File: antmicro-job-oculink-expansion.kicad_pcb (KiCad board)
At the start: 4 copper layers, 20 x 60 mm, 25 parts, among them J1 OCuLink_x4_Amphenol_G14A42121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, J2 Plug_Samtec_ERM8_2x40_ERM8-04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, U1 MAX3373EEKA+

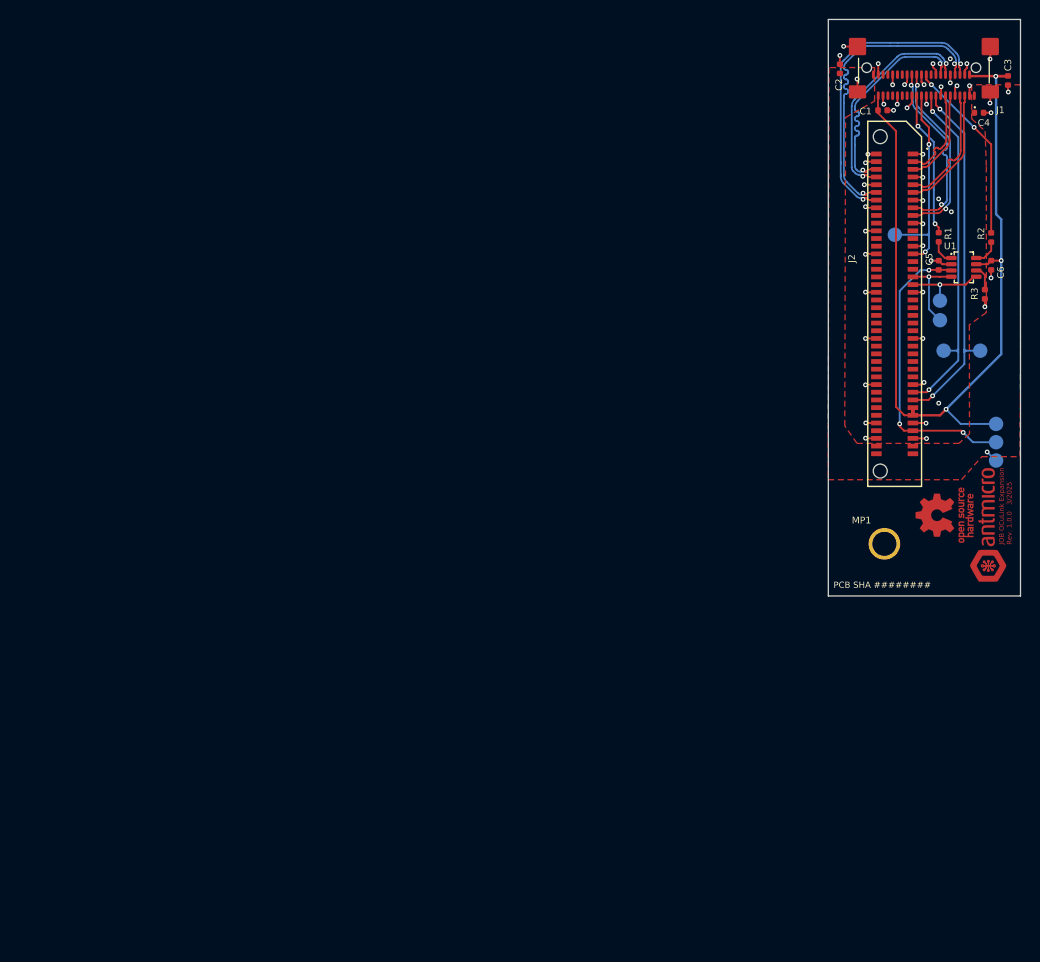
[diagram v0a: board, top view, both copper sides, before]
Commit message: [#74340] Update component placement
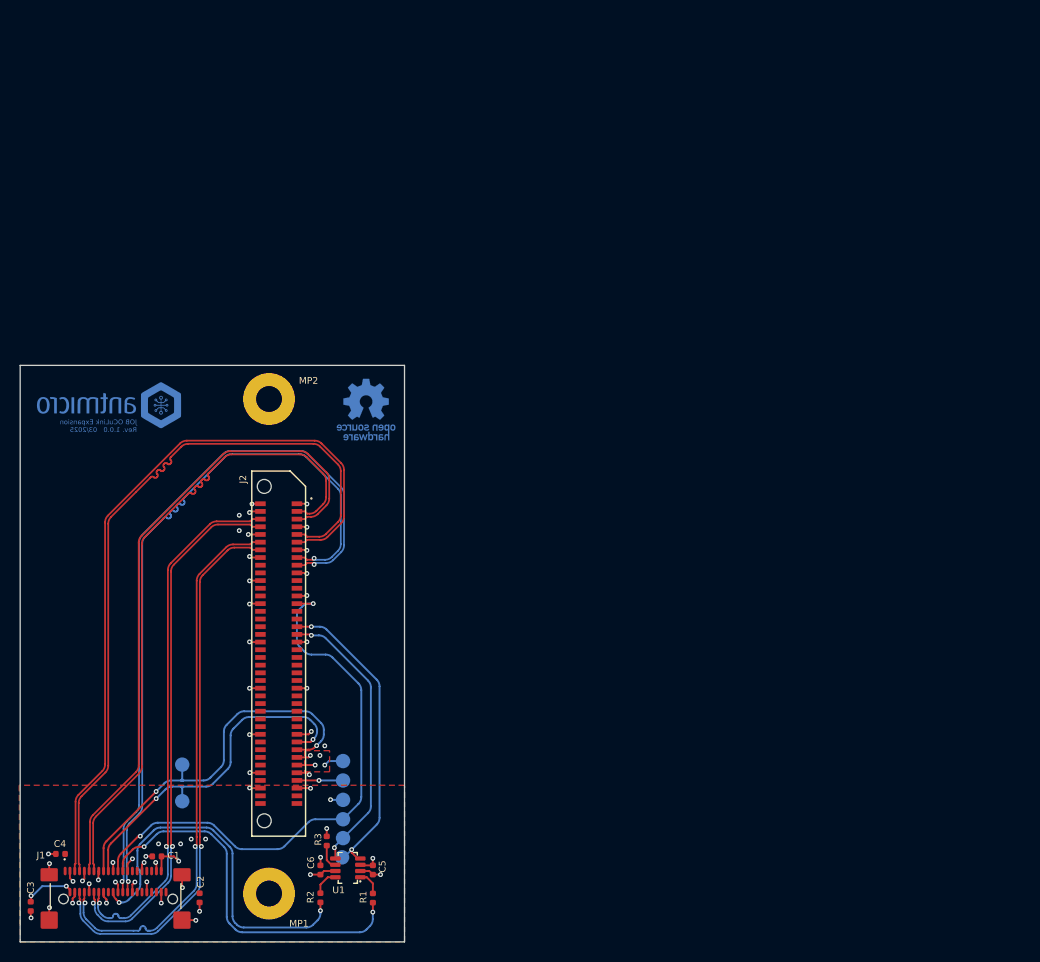
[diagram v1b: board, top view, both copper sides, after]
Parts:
- removed G***: LOGO, antmicro-footprints:antmicro-logo_scaled_12mm_mask
- removed REF**: OSHW-Logo_5.7x6mm_Copper, antmicro-footprints:OSHW-Logo_5.7x6mm_Copper
- removed REF**: LOGO, antmicro-footprints:antmicro-logo_scaled_12mm
- removed REF**: OSHW-Logo_5.7x6mm_Mask, antmicro-footprints:OSHW-Logo_5.7x6mm_Mask
- added MP2: MP_Pad5.4mm_Drill2.7mm, antmicro-footprints:MP_Pad5.4mm_Drill2.7mm, F.Cu at (135.9, 93.5)
- added N1: oshw_logo, antmicro-footprints:oshw-logo, B.Cu at (146.0, 94.6)
- added N2: antmicro_logo, antmicro-footprints:antmicro-logo_scaled_15mm, B.Cu at (118.8, 94.2)
- MP1: value MP_Pad3.3mm_Drill2.5mm -> MP_Pad5.4mm_Drill2.7mm; footprint antmicro-footprints:MP_Pad3.3mm_Drill2.5mm -> antmicro-footprints:MP_Pad5.4mm_Drill2.7mm
- moved C3 133.2 mm to (111.1, 146.3)
- moved C4 122.8 mm to (114.2, 140.8), turned to 0 degrees
- moved J1 122.7 mm to (119.9, 146.9), turned to 0 degrees
- moved C2 109.0 mm to (128.7, 145.4), turned to 90 degrees
- moved C1 108.3 mm to (124.2, 141.1), turned to 0 degrees
- moved R2 98.0 mm to (141.2, 145.4), turned to -90 degrees
- moved C6 94.0 mm to (141.2, 142.5), turned to -90 degrees
- moved TP1 93.6 mm to (126.9, 131.6), turned to -90 degrees
- moved TP2 92.1 mm to (126.9, 135.4), turned to -90 degrees
- moved R1 90.5 mm to (146.7, 145.4), turned to -90 degrees
- moved U1 89.5 mm to (144.1, 142.3), turned to 180 degrees
- moved R3 89.0 mm to (141.9, 139.5), turned to -90 degrees
- moved C5 86.2 mm to (146.7, 142.5), turned to 90 degrees
- moved TP7 83.7 mm to (143.6, 137.2)
- moved TP5 83.6 mm to (143.5, 141.2)
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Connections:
- net /~{PCIE_CPRSNT} renamed /~{CPRSNT}
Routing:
- net +3.3V: track 91.0 -> 17.1 mm, vias 3 -> 8
- net /PCIE_TX0+: track 13.1 -> 78.4 mm
- net /PCIE_TX0-: track 13.0 -> 78.3 mm
- net /PCIE_TX1+: track 9.90 -> 67.9 mm
- net /PCIE_TX1-: track 9.87 -> 67.8 mm
- net /PCIE_CLK+: track 19.3 -> 75.8 mm
- net /PCIE_CLK-: track 19.2 -> 75.7 mm
- net /~{PCIE_RST}: track 22.0 -> 58.4 mm
- net /PCIE_RX1-: track 23.4 -> 55.9 mm
- net /PCIE_RX1+: track 23.5 -> 56.0 mm
- net /PCIE_RX0-: track 32.4 -> 57.8 mm
- net /PCIE_RX0+: track 32.5 -> 57.8 mm
- net +1V8: track 31.2 -> 6.97 mm, vias 3 -> 2
- net Net-(J1-~{CPRSNT}): track 15.2 -> 39.2 mm
- net /JOB_GPIO07: track 9.18 -> 32.6 mm, vias 1 -> 2
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- added copper zone on In1.Cu, net +1V8
- added copper zone on F.Cu, net +3.3V
- added copper zone on In1.Cu, net +3.3V
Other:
- board size 20 x 60 mm -> 40 x 60 mm
- board text added: "JOB OCuLink Expansion Rev. ${REVISION} 03/2025"
- board text added: "OCuLink PCie x2"
- board text removed: "JOB OCuLink Expansion Rev. ${REVISION} 3/2025"

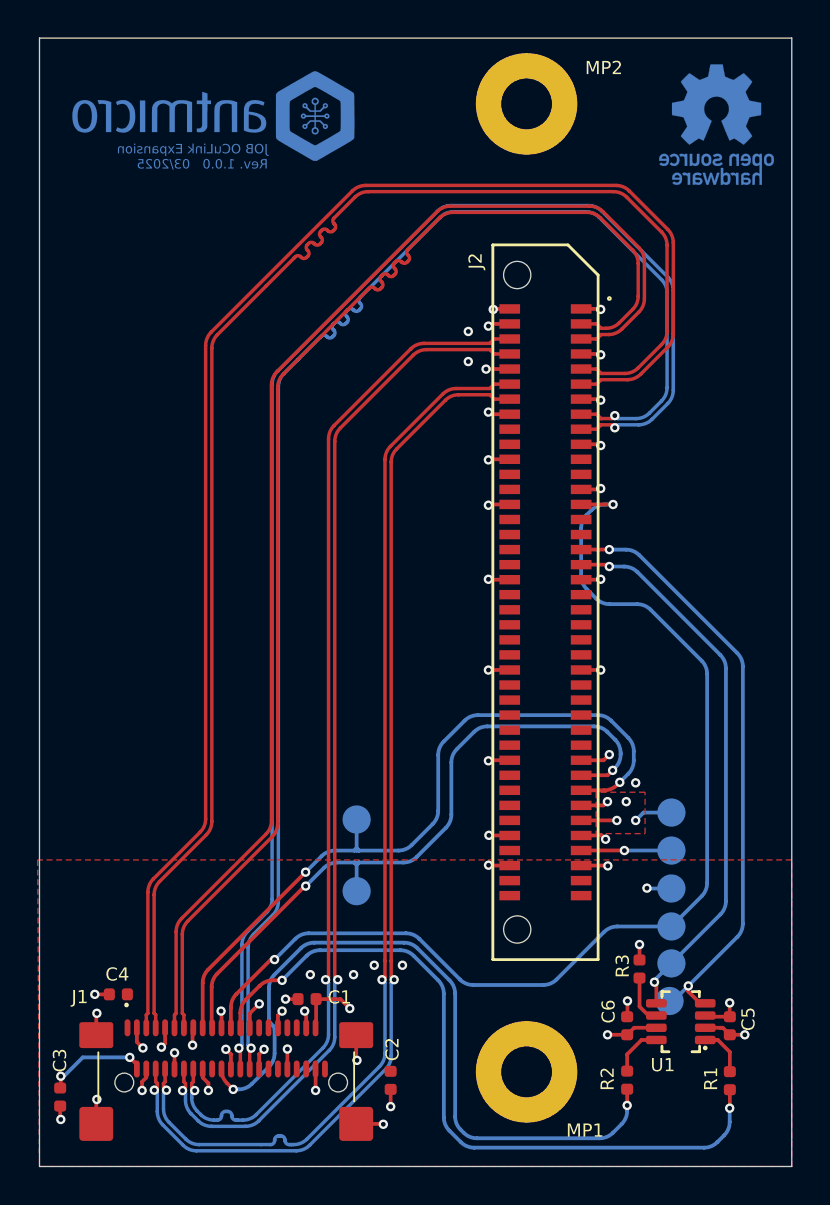
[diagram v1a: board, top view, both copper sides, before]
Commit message: [#74340] Finalize layout and add GND  plane stiching
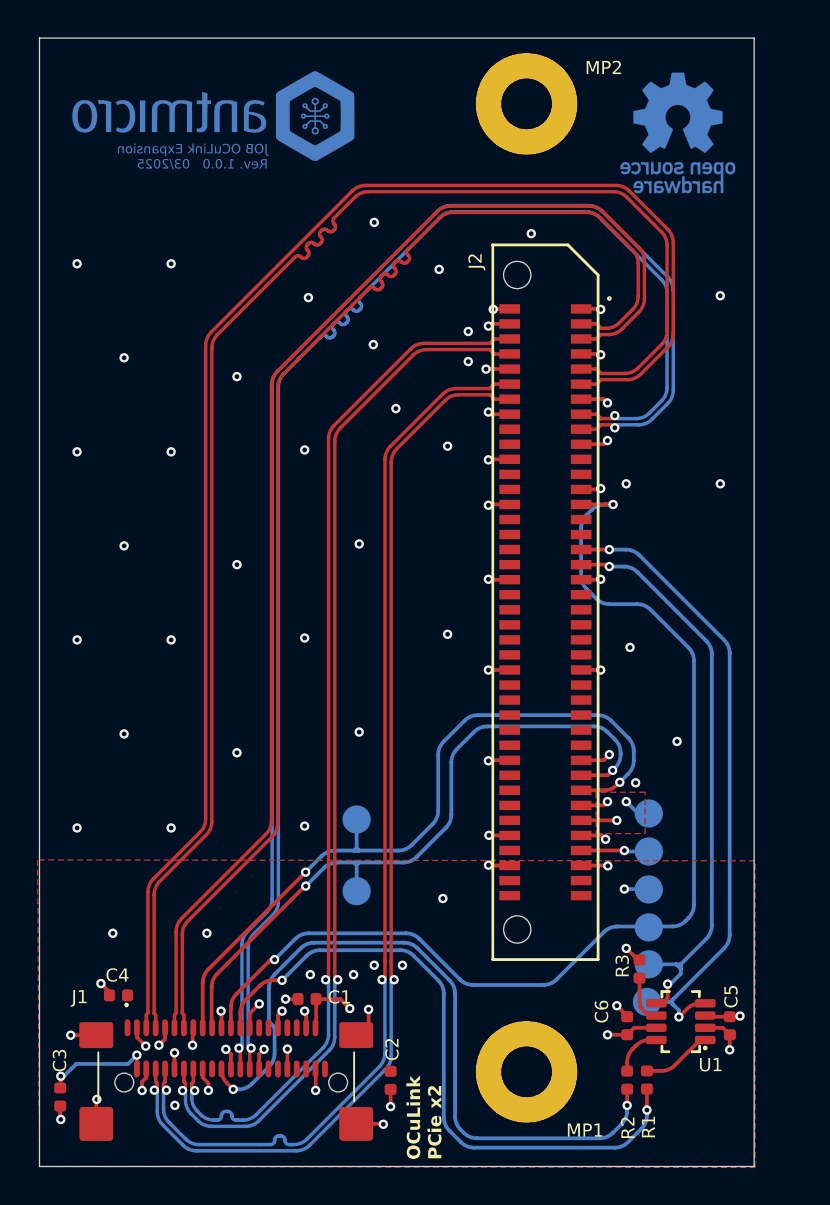
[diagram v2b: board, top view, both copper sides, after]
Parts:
- moved R1 4.41 mm to (142.3, 145.4)
- moved N1 2.10 mm to (143.9, 95.0)
- moved TP10 1.20 mm to (142.4, 133.2)
- moved TP5 1.20 mm to (142.3, 141.2)
- moved TP6 1.20 mm to (142.4, 139.2)
- moved TP7 1.20 mm to (142.4, 137.3)
- moved TP8 1.20 mm to (142.4, 131.2)
- moved TP9 1.20 mm to (142.4, 135.3)
- moved C4 0.05 mm to (114.2, 140.9)
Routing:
- net Net-(J1-~{CPRSNT}): track 39.2 -> 34.6 mm
- net /JOB_GPIO07: track 32.6 -> 34.7 mm
- net GND: track 52.3 -> 53.7 mm, vias 53 -> 89
- net +1V8: track 6.97 -> 5.61 mm
- net /JOB_GPIO09: track 29.8 -> 31.1 mm
- net /~{CPRSNT}: track 2.62 -> 3.73 mm
- net +3.3V: track 17.1 -> 16.8 mm, vias 8 -> 7
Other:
- board size 40 x 60 mm -> 38 x 60 mm

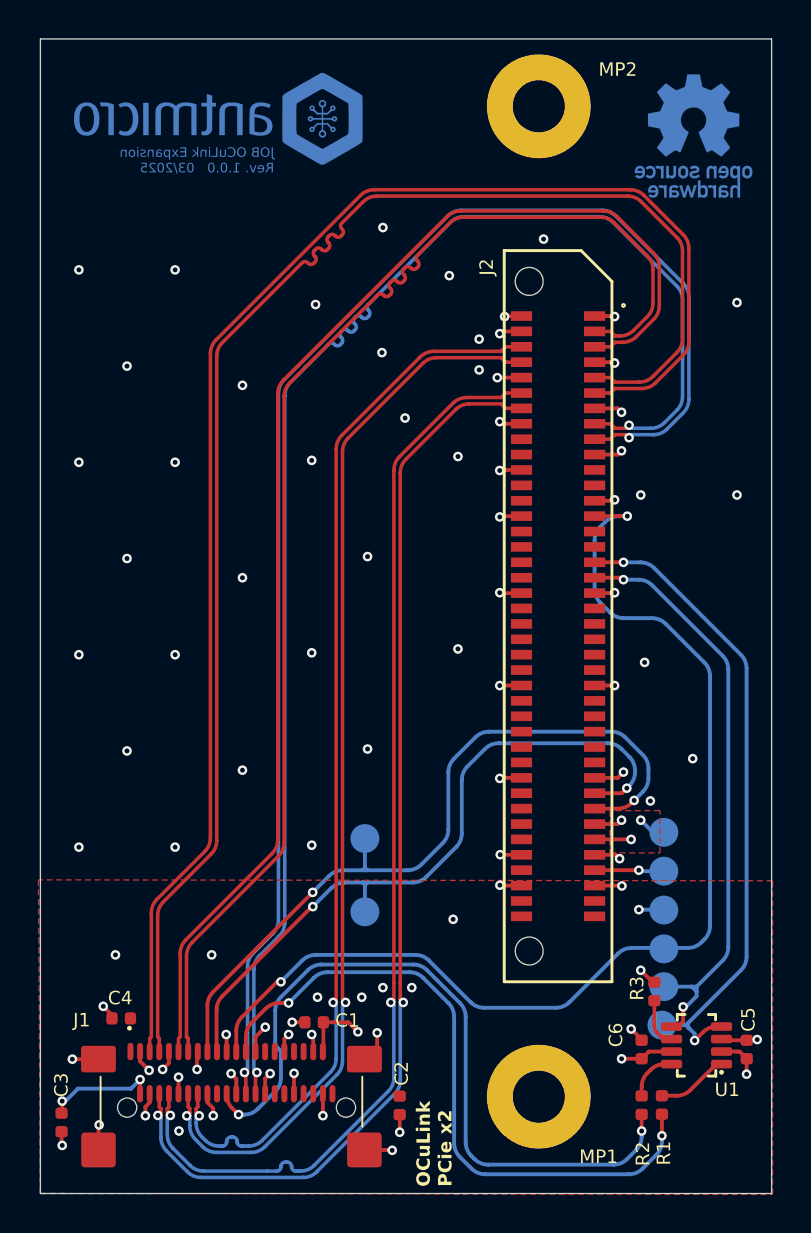
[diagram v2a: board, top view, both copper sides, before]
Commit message: [#74340] Add logos on both sides of PCB
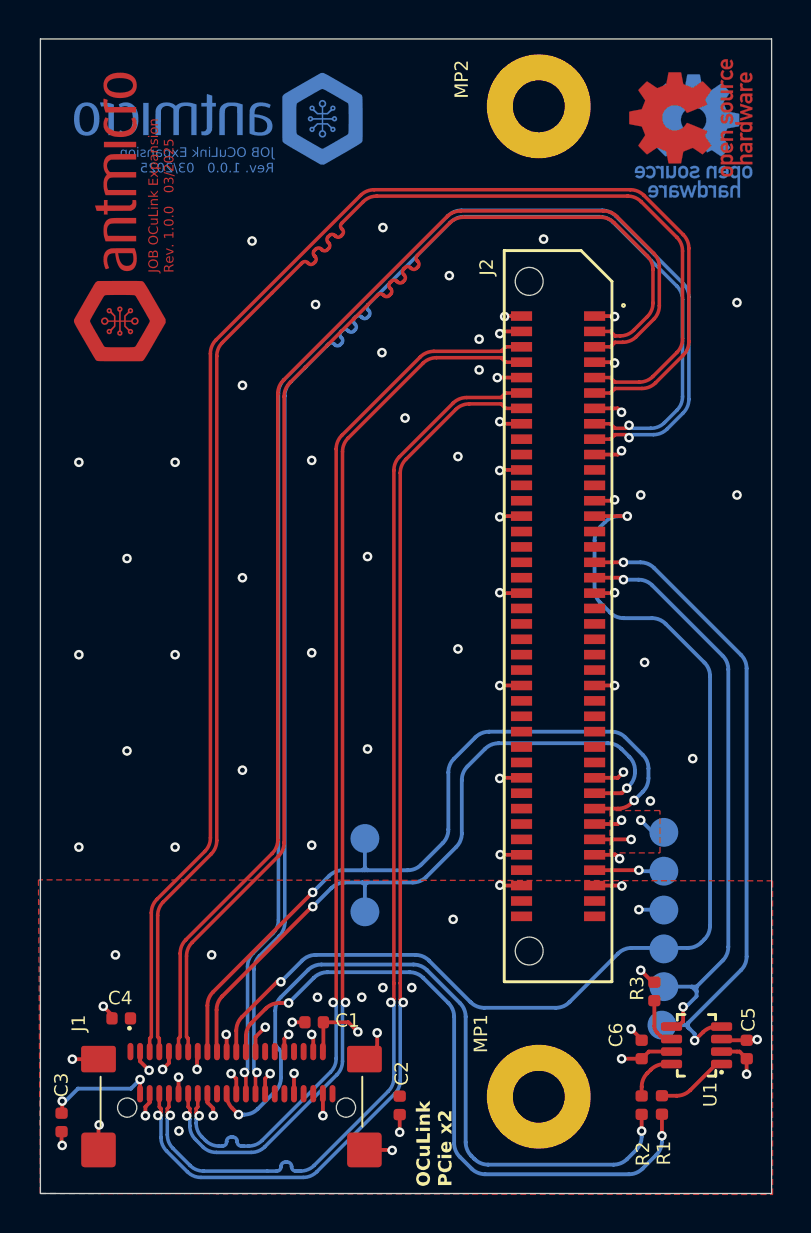
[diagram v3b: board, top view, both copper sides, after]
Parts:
- added N1: oshw_logo, antmicro-footprints:oshw-logo, F.Cu at (143.8, 94.1)
- added N2: antmicro_logo, antmicro-footprints:antmicro-logo_scaled_15mm, F.Cu at (114.2, 98.8)
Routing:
- net GND: vias 89 -> 87

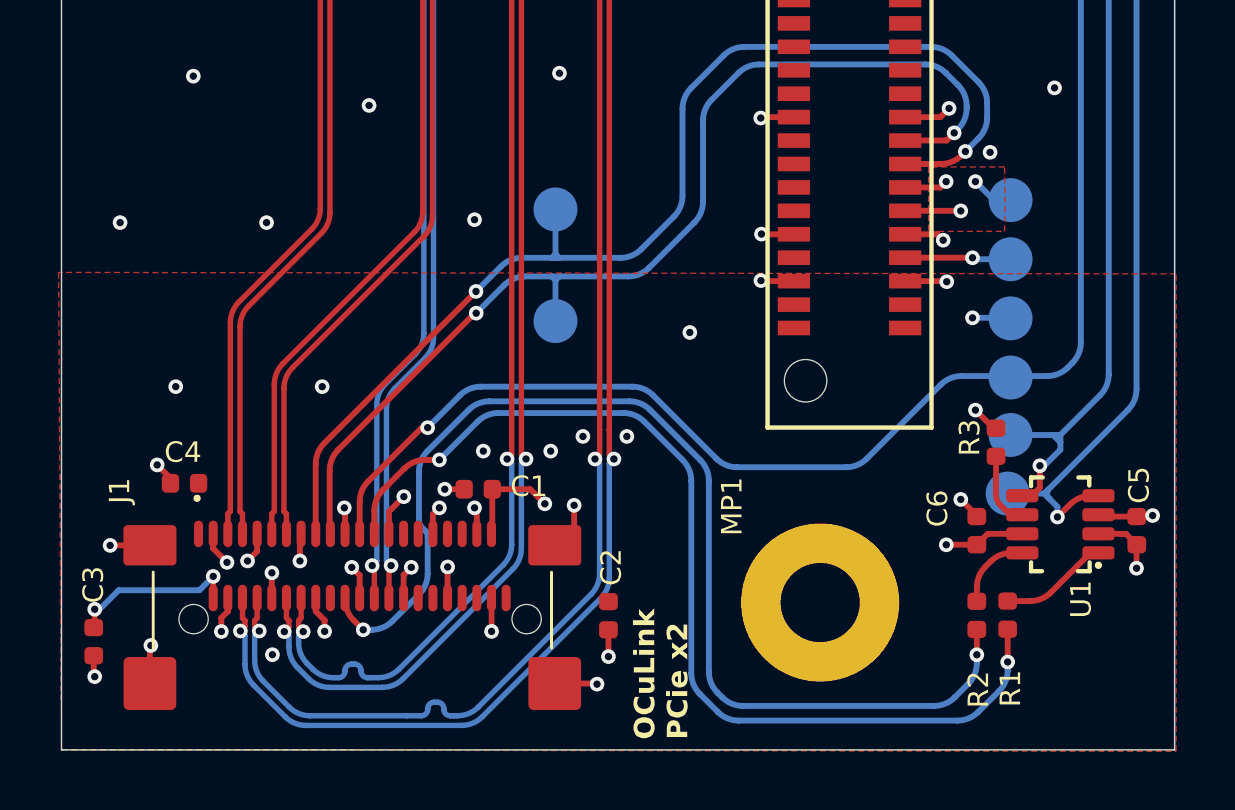
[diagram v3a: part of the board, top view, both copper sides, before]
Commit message: [#74340] Add minor power plane adjustments
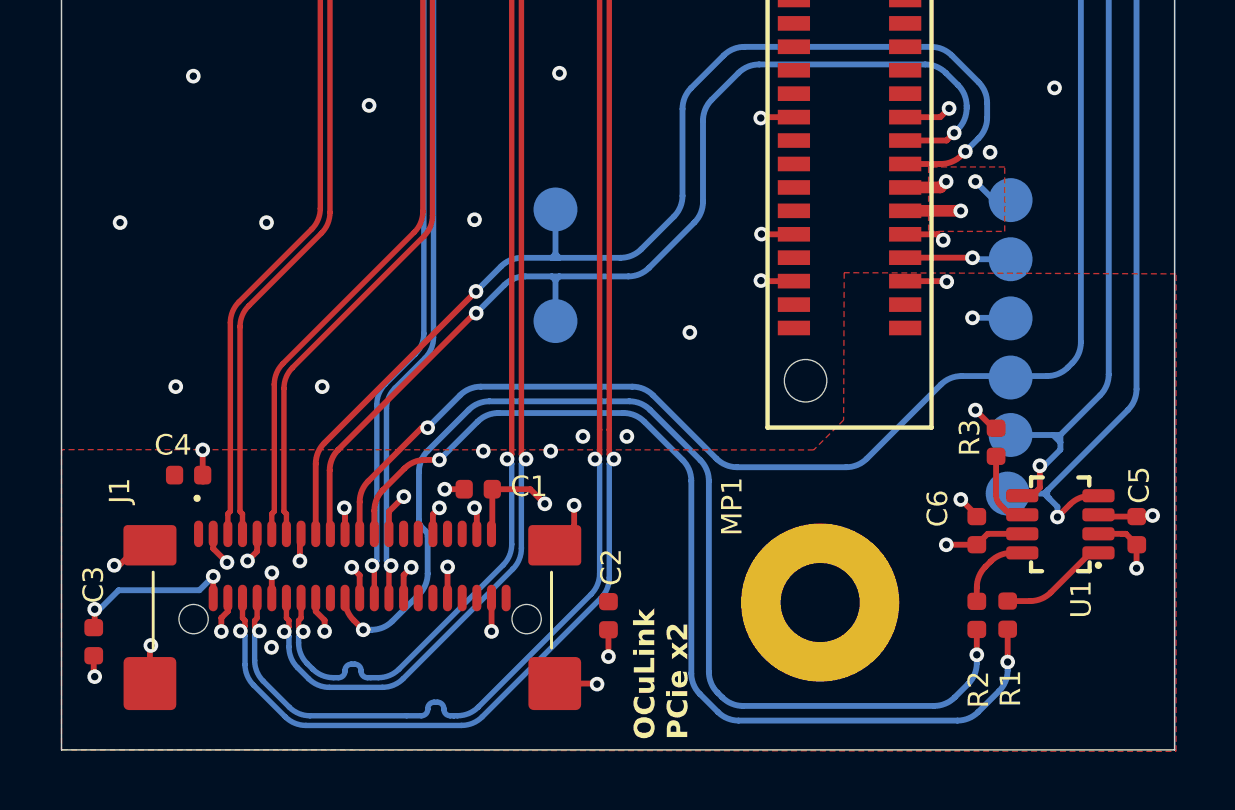
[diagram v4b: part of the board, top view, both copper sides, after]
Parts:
- moved C4 0.31 mm to (114.3, 140.6), turned to 180 degrees
- renumbered N1 to N3, N2 to N4
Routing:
- net GND: track 53.7 -> 54.3 mm
